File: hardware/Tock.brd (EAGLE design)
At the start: 100 x 80 mm, 37 parts, among them IC1 NE555D, IC2 LM7805, IC3 AVR-MEGA8-PPTH, IC4 MCP1700-33, J2 ISP, J4 VIN, Y1 16MHz

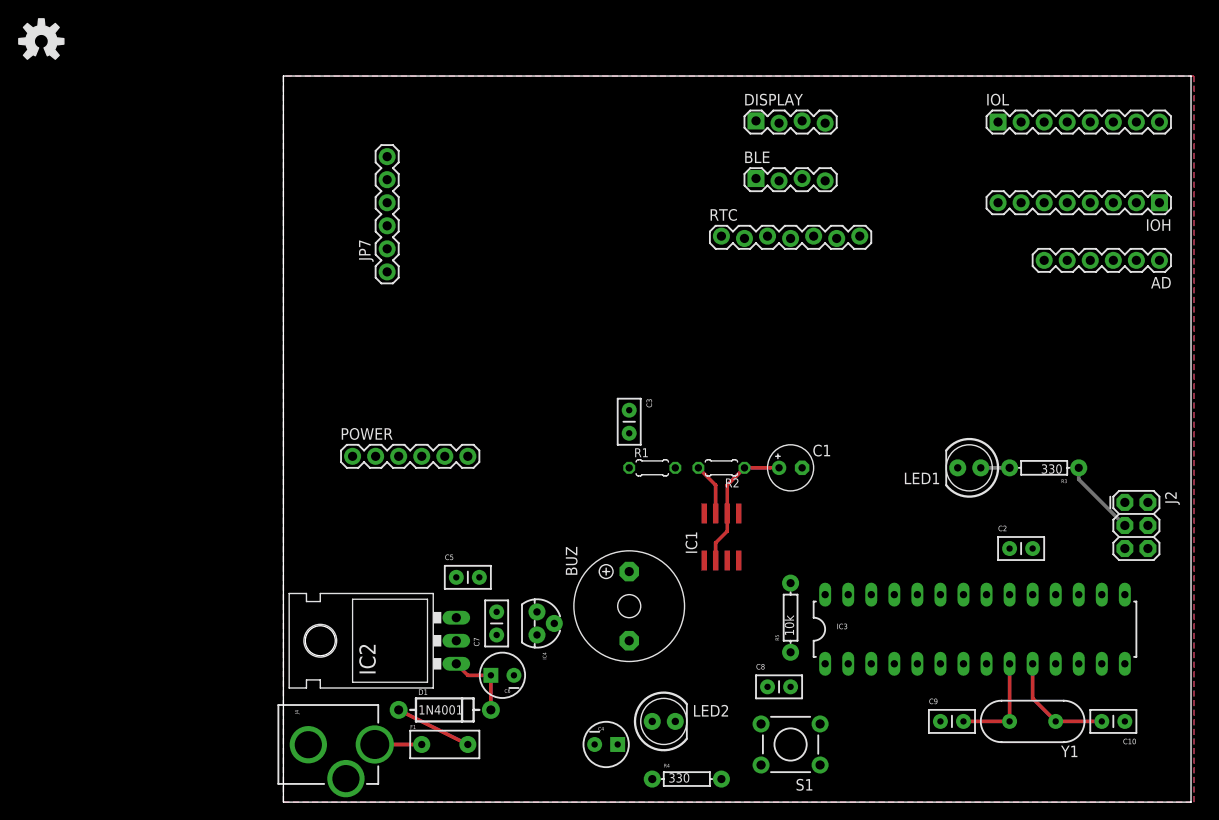
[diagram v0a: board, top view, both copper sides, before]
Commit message: Update hardware
Remove extra bit-packing code and switch to standard library macros
Encapsulate enums
Add WIP BOM and more information to readme
Finish routing hardware
Switch to SMD capacitors and resistors
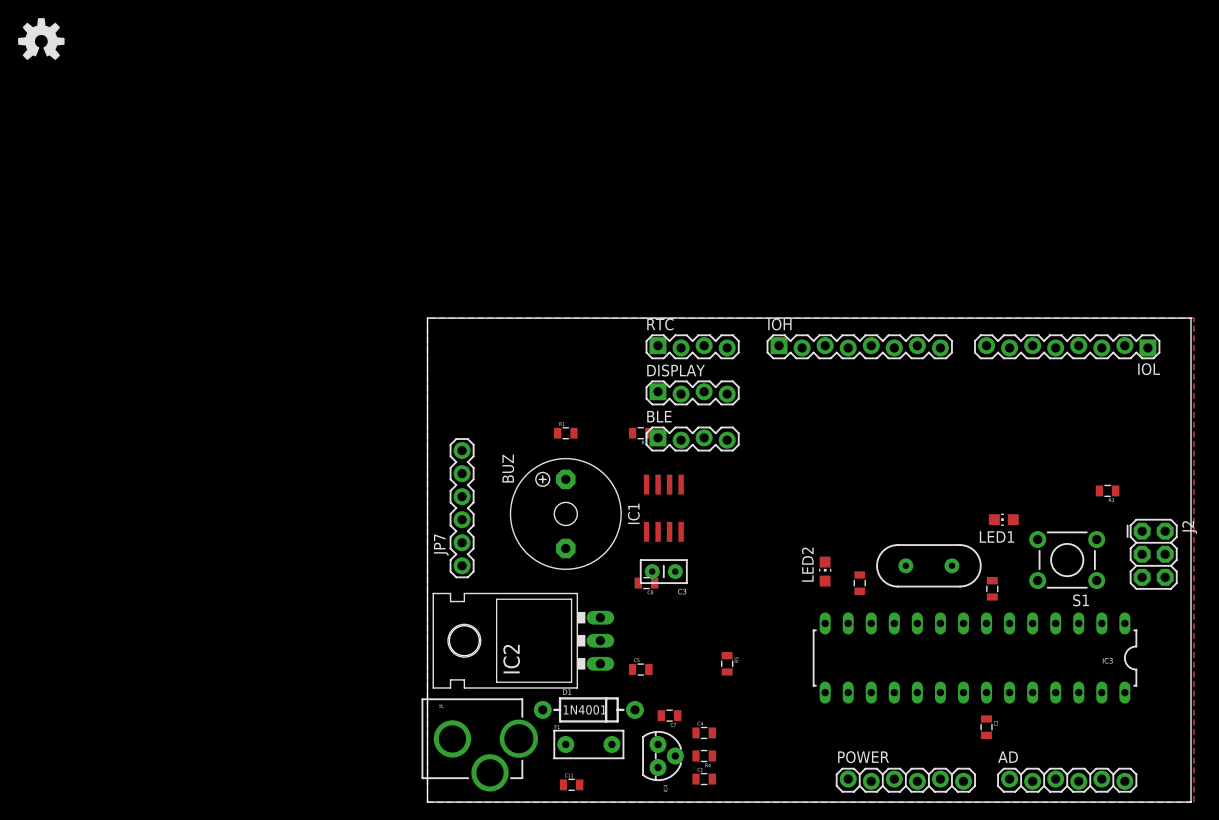
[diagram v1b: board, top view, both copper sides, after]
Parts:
- removed C6: 10uF, SparkFun:CPOL-RADIAL-10UF-25V
- added C11: 220uf, SparkFun-Passives:0805
- AD, POWER: device SparkFun:1X06 -> SparkFun-Connectors:1X06_LOCK
- C1: value 220uf -> 10uf; device rcl:E2,5-5 -> SparkFun-Passives:0805
- C10, C2, C5, C7, C8, C9: device SparkFun:CAP-PTH-SMALL2 -> SparkFun-Passives:0805
- C4: value 10uF -> 10uf; device SparkFun:CPOL-RADIAL-10UF-25V -> SparkFun-Passives:0805
- IOH, IOL: device SparkFun:1X08 -> SparkFun-Connectors:1X08_LOCK
- LED1, LED2: device SparkFun:LED5MM -> led:CHIP-LED0805
- R1, R2: device rcl:0204/5 -> SparkFun-Resistors:0805
- R3, R4, R5: device SparkFun:AXIAL-0.3 -> SparkFun-Resistors:0805
- RTC: device SparkFun-Connectors:1X07_LOCK -> SparkFun-Connectors:1X04_LOCK
- moved POWER 65.2 mm to (62.2, 2.54)
- moved AD 59.5 mm to (80.0, 2.54), turned to 0 degrees
- moved IOH 44.8 mm to (54.6, 50.2), turned to 0 degrees
- moved S1 36.6 mm to (86.4, 26.7)
- moved C1 35.6 mm to (46.4, 2.54)
- moved JP7 33.4 mm to (19.7, 26.0)
- moved C10 32.9 mm to (63.5, 24.1), turned to 90 degrees
- moved DISPLAY 31.7 mm to (41.3, 45.1)
- moved BLE 30.5 mm to (41.3, 40.0)
- moved IOL 29.8 mm to (95.2, 50.2), turned to 180 degrees
- moved LED2 24.3 mm to (59.7, 25.4)
- moved C5 22.7 mm to (39.4, 14.6)
- moved C7 21.0 mm to (42.5, 9.53), turned to 180 degrees
- moved Y1 20.6 mm to (71.1, 26.0), turned to 0 degrees
- moved C2 19.8 mm to (77.5, 8.26), turned to 270 degrees
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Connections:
- net 5V: now also R4.2, R5.2, RTC.3; no longer R4.P$2, R5.P$2, RTC.5
- net GND: now also C1.2, C11.2, LED1.C, LED2.C, RTC.4; no longer C1.-, C6.2, LED1.K, LED2.K, RTC.6
- net MISO: now also RTC.2; no longer RTC.4
- net MOSI: now also RTC.1; no longer RTC.3
- net N$1: now also R3.2; no longer R3.P$2
- net N$2: now also R4.1; no longer R4.P$1
- net N$5: now also C11.1; no longer C1.+
- net RESET: now also R5.1; no longer R5.P$1
- net SCK: now also R3.1; no longer R3.P$1
- net VIN: now also C1.1; no longer C6.1
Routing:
- net N$5: track 15.3 -> 0.00 mm
- net N$4: track 12.5 -> 0.00 mm
- net N$3: track 11.4 -> 0.00 mm
- net N$6: track 8.52 -> 0.00 mm
- net SCK: track 8.45 -> 0.00 mm
- net VIN: track 8.15 -> 0.00 mm
- net N$9: track 5.81 -> 0.00 mm
- net RAW: track 5.17 -> 0.00 mm
- net N$1: track 3.18 -> 0.00 mm
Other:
- board size 100 x 80 mm -> 84.1 x 53.3 mm

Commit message: Shrink board footprint further
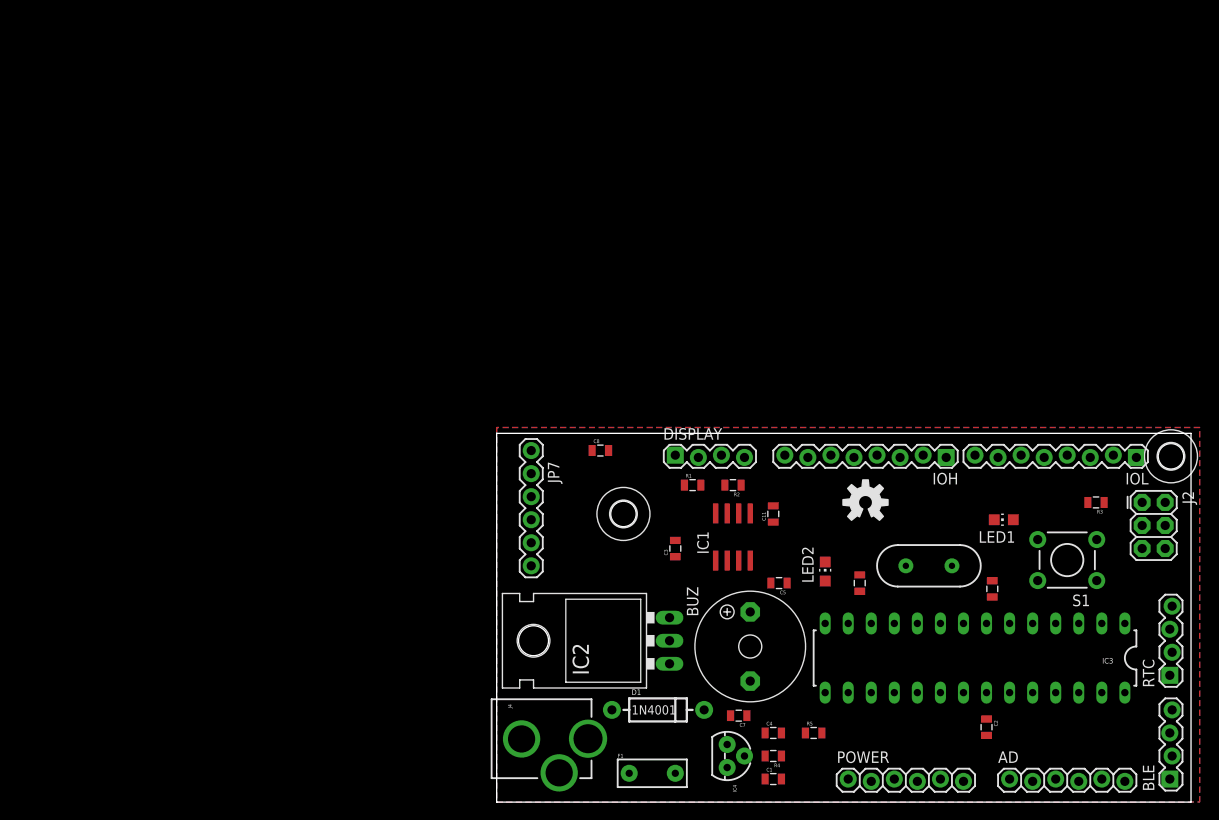
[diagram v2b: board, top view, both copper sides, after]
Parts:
- added U$10, U$8: (no value), holes:2,8
- C3: device SparkFun:CAP-PTH-SMALL2 -> SparkFun-Capacitors:0805
- moved U$7 104.0 mm to (64.1, 33.0)
- moved BLE 67.8 mm to (97.8, 2.54), turned to 90 degrees
- moved RTC 67.1 mm to (97.8, 14.0), turned to 90 degrees
- moved C11 37.2 mm to (54.0, 31.8), turned to 90 degrees
- moved BUZ 25.0 mm to (51.4, 17.1)
- moved IOH 22.0 mm to (73.0, 38.1), turned to 180 degrees
- moved C5 18.0 mm to (54.6, 24.1), turned to 180 degrees
- moved C8 15.5 mm to (34.9, 38.7), turned to 0 degrees
- moved R1 15.1 mm to (45.1, 34.9)
- moved JP7 14.8 mm to (27.3, 38.7), turned to 270 degrees
- moved R5 12.2 mm to (58.4, 7.62), turned to 0 degrees
- moved IOL 12.1 mm to (94.0, 38.1)
- moved R2 11.7 mm to (49.5, 34.9)
- moved IC1 8.26 mm to (49.5, 29.2)
- moved F1 7.67 mm to (40.6, 3.17)
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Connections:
- removed net IO2: IC3.4, IOL.3
- new net 555RST: IC1.4, IC3.4, IOL.3
- net 5V: no longer IC1.4
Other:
- board size 84.1 x 53.3 mm -> 76.5 x 40.6 mm

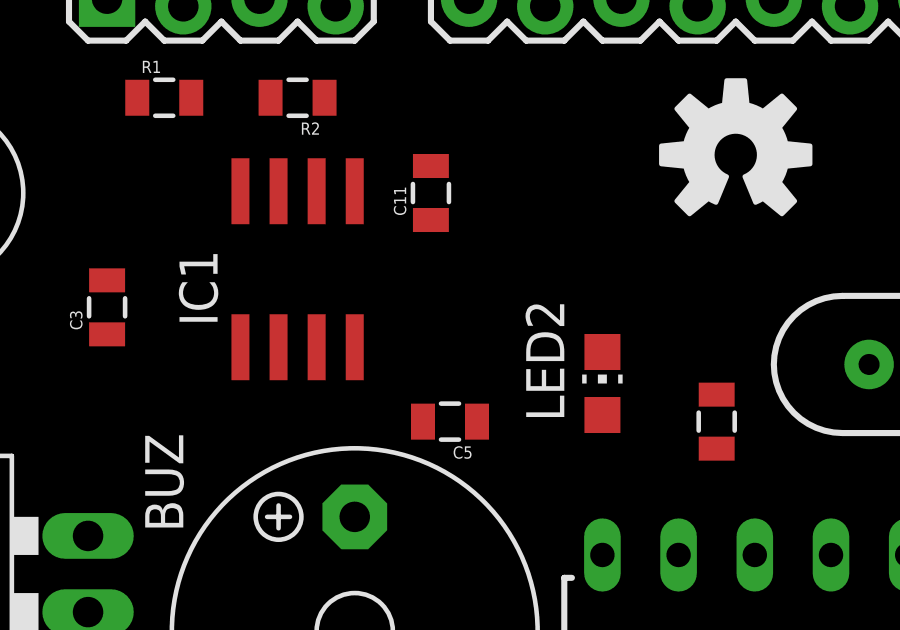
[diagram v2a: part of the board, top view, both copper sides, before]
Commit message: Integrate with latest Tick app
Fix 555 timer sub circuit control pin
Fix GetSetting command message
Fix out of sync enum values
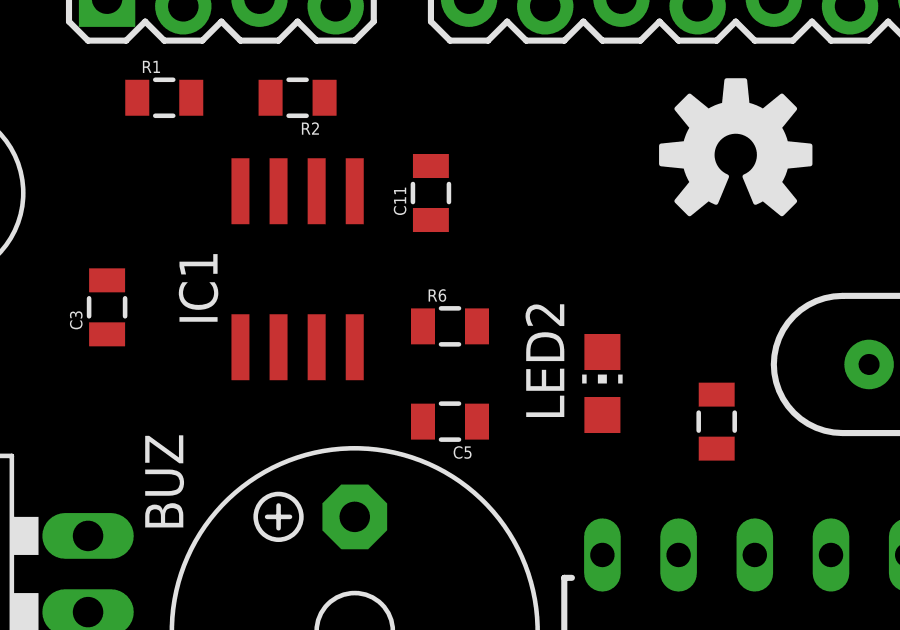
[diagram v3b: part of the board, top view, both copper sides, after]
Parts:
- added R6: 10K, SparkFun-Resistors:0805
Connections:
- net 555RST: now also R6.2
- net 5V: no longer BUZ.+
- net GND: now also BUZ.-, R6.1
- net N$7: now also BUZ.+; no longer BUZ.-
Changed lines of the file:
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@@
 <element name="U$8" library="holes" package="2,8" value="" x="97.79" y="38.1"/>
 <element name="U$10" library="holes" package="2,8" value="" x="37.465" y="31.75"/>
+<element name="R6" library="SparkFun-Resistors" package="0805" value="10K" x="54.61" y="27.305">
+<attribute name="PROD_ID" value="RES-11622" x="54.61" y="27.305" size="1.778" layer="27" display="off"/>
+</element>
 </elements>
 <signals>
@@
 <contactref element="IC1" pad="8"/>
 <contactref element="R1" pad="1"/>
-<contactref element="BUZ" pad="+"/>
 <contactref element="BLE" pad="4"/>
 <contactref element="DISPLAY" pad="4"/>
@@
 <wire x1="53.075" y1="5.08" x2="53.075" y2="7.62" width="0" layer="19" extent="1-1"/>
 <wire x1="50.8" y1="5.08" x2="53.075" y2="5.08" width="0" layer="19" extent="1-1"/>
-<wire x1="51.435" y1="20.955" x2="53.075" y2="7.62" width="0" layer="19" extent="1-1"/>
-<wire x1="55.51" y1="24.13" x2="51.435" y2="20.955" width="0" layer="19" extent="1-1"/>
-<wire x1="42.545" y1="20.32" x2="51.435" y2="20.955" width="0" layer="19" extent="1-1"/>
+<wire x1="42.545" y1="20.32" x2="53.075" y2="7.62" width="0" layer="19" extent="1-1"/>
 <wire x1="43.18" y1="28.84" x2="42.545" y2="20.32" width="0" layer="19" extent="1-1"/>
 <wire x1="47.625" y1="31.81" x2="43.18" y2="28.84" width="0" layer="19" extent="1-1"/>
 <wire x1="44.185" y1="34.925" x2="47.625" y2="31.81" width="0" layer="19" extent="1-1"/>
 <wire x1="50.8" y1="37.973" x2="47.625" y2="31.81" width="0" layer="19" extent="1-1"/>
+<wire x1="55.51" y1="24.13" x2="47.625" y2="31.81" width="0" layer="19" extent="1-1"/>
 <wire x1="27.305" y1="31.115" x2="43.18" y2="28.84" width="0" layer="19" extent="1-1"/>
 </signal>
@@
 <contactref element="C1" pad="2"/>
 <contactref element="C4" pad="2"/>
+<contactref element="R6" pad="1"/>
+<contactref element="BUZ" pad="-"/>
+<wire x1="97.917" y1="21.59" x2="97.155" y2="27.94" width="0" layer="19" extent="1-1"/>
+<wire x1="89.6112" y1="24.4094" x2="97.155" y2="27.94" width="0" layer="19" extent="1-1"/>
+<wire x1="83.1088" y1="24.4094" x2="89.6112" y2="24.4094" width="0" layer="19" extent="1-1"/>
+<wire x1="78.105" y1="22.595" x2="83.1088" y2="24.4094" width="0" layer="19" extent="1-1"/>
+<wire x1="74.93" y1="19.685" x2="78.105" y2="22.595" width="0" layer="19" extent="1-1"/>
+<wire x1="77.47" y1="12.065" x2="74.93" y2="19.685" width="0" layer="19" extent="1-1"/>
+<wire x1="77.47" y1="7.355" x2="77.47" y2="12.065" width="0" layer="19" extent="1-1"/>
+<wire x1="72.39" y1="2.54" x2="77.47" y2="7.355" width="0" layer="19" extent="1-1"/>
+<wire x1="69.85" y1="2.286" x2="72.39" y2="2.54" width="0" layer="19" extent="1-1"/>
+<wire x1="78.325" y1="31.115" x2="83.1088" y2="24.4094" width="0" layer="19" extent="1-1"/>
+<wire x1="63.5" y1="23.23" x2="74.93" y2="19.685" width="0" layer="19" extent="1-1"/>
+<wire x1="59.69" y1="26.45" x2="63.5" y2="23.23" width="0" layer="19" extent="1-1"/>
+<wire x1="53.71" y1="24.13" x2="59.69" y2="26.45" width="0" layer="19" extent="1-1"/>
+<wire x1="47.625" y1="26.61" x2="53.71" y2="24.13" width="0" layer="19" extent="1-1"/>
+<wire x1="43.18" y1="27.04" x2="47.625" y2="26.61" width="0" layer="19" extent="1-1"/>
+<wire x1="53.975" y1="32.65" x2="59.69" y2="26.45" width="0" layer="19" extent="1-1"/>
+<wire x1="57.785" y1="37.973" x2="53.975" y2="32.65" width="0" layer="19" extent="1-1"/>
+<wire x1="48.26" y1="38.227" x2="53.975" y2="32.65" width="0" layer="19" extent="1-1"/>
+<wire x1="42.545" y1="17.78" x2="43.18" y2="27.04" width="0" layer="19" extent="1-1"/>
+<wire x1="51.435" y1="13.335" x2="42.545" y2="17.78" width="0" layer="19" extent="1-1"/>
+<wire x1="49.265" y1="9.525" x2="51.435" y2="13.335" width="0" layer="19" extent="1-1"/>
+<wire x1="48.895" y1="6.35" x2="49.265" y2="9.525" width="0" layer="19" extent="1-1"/>
+<wire x1="54.875" y1="7.62" x2="49.265" y2="9.525" width="0" layer="19" extent="1-1"/>
+<wire x1="54.875" y1="2.54" x2="54.875" y2="7.62" width="0" layer="19" extent="1-1"/>
+<wire x1="27.305" y1="26.035" x2="43.18" y2="27.04" width="0" layer="19" extent="1-1"/>
+<wire x1="27.305" y1="28.575" x2="27.305" y2="26.035" width="0" layer="19" extent="1-1"/>
+<wire x1="30.385" y1="3.2234" x2="48.895" y2="6.35" width="0" layer="19" extent="1-1"/>
+<wire x1="26.242" y1="6.9596" x2="30.385" y2="3.2234" width="0" layer="19" extent="1-1"/>
+<wire x1="53.71" y1="27.305" x2="26.242" y2="6.9596" width="0" layer="19" extent="1-1"/>
+<wire x1="97.663" y1="2.54" x2="97.917" y2="21.59" width="0" layer="19" extent="1-1"/>
 </signal>
 <signal name="RESET">
@@
 <signal name="N$7">
 <contactref element="IC1" pad="3"/>
-<contactref element="BUZ" pad="-"/>
-<wire x1="51.435" y1="13.335" x2="50.165" y2="26.61" width="0" layer="19" extent="1-1"/>
+<contactref element="BUZ" pad="+"/>
+<wire x1="51.435" y1="20.955" x2="50.165" y2="26.61" width="0" layer="19" extent="1-1"/>
 </signal>
 <signal name="555RST">
@@
 <contactref element="IOL" pad="3"/>
 <contactref element="IC3" pad="4"/>
+<contactref element="R6" pad="2"/>
 <wire x1="85.09" y1="19.685" x2="88.9" y2="37.973" width="0" layer="19" extent="1-1"/>
 <wire x1="51.435" y1="26.61" x2="85.09" y2="19.685" width="0" layer="19" extent="1-1"/>
+<wire x1="55.51" y1="27.305" x2="51.435" y2="26.61" width="0" layer="19" extent="1-1"/>
 </signal>
 </signals>
